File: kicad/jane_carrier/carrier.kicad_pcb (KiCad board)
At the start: 4 copper layers, 162.6 x 114.3 mm, 112 parts, among them CON1 EDSTL130_02, CON2 BNC_361V504EFT, CON3 BNC_361V504EFT, CON4 BNC_361V504EFT, CON5 BNC_361V504EFT, P1 61083-101400LF, P2 61083-101400LF, U1 STM6779LWB6F, U2 XCL214B333DR, U3 XCL214B333DR, U4 ADCMP552, U5 ADCMP552

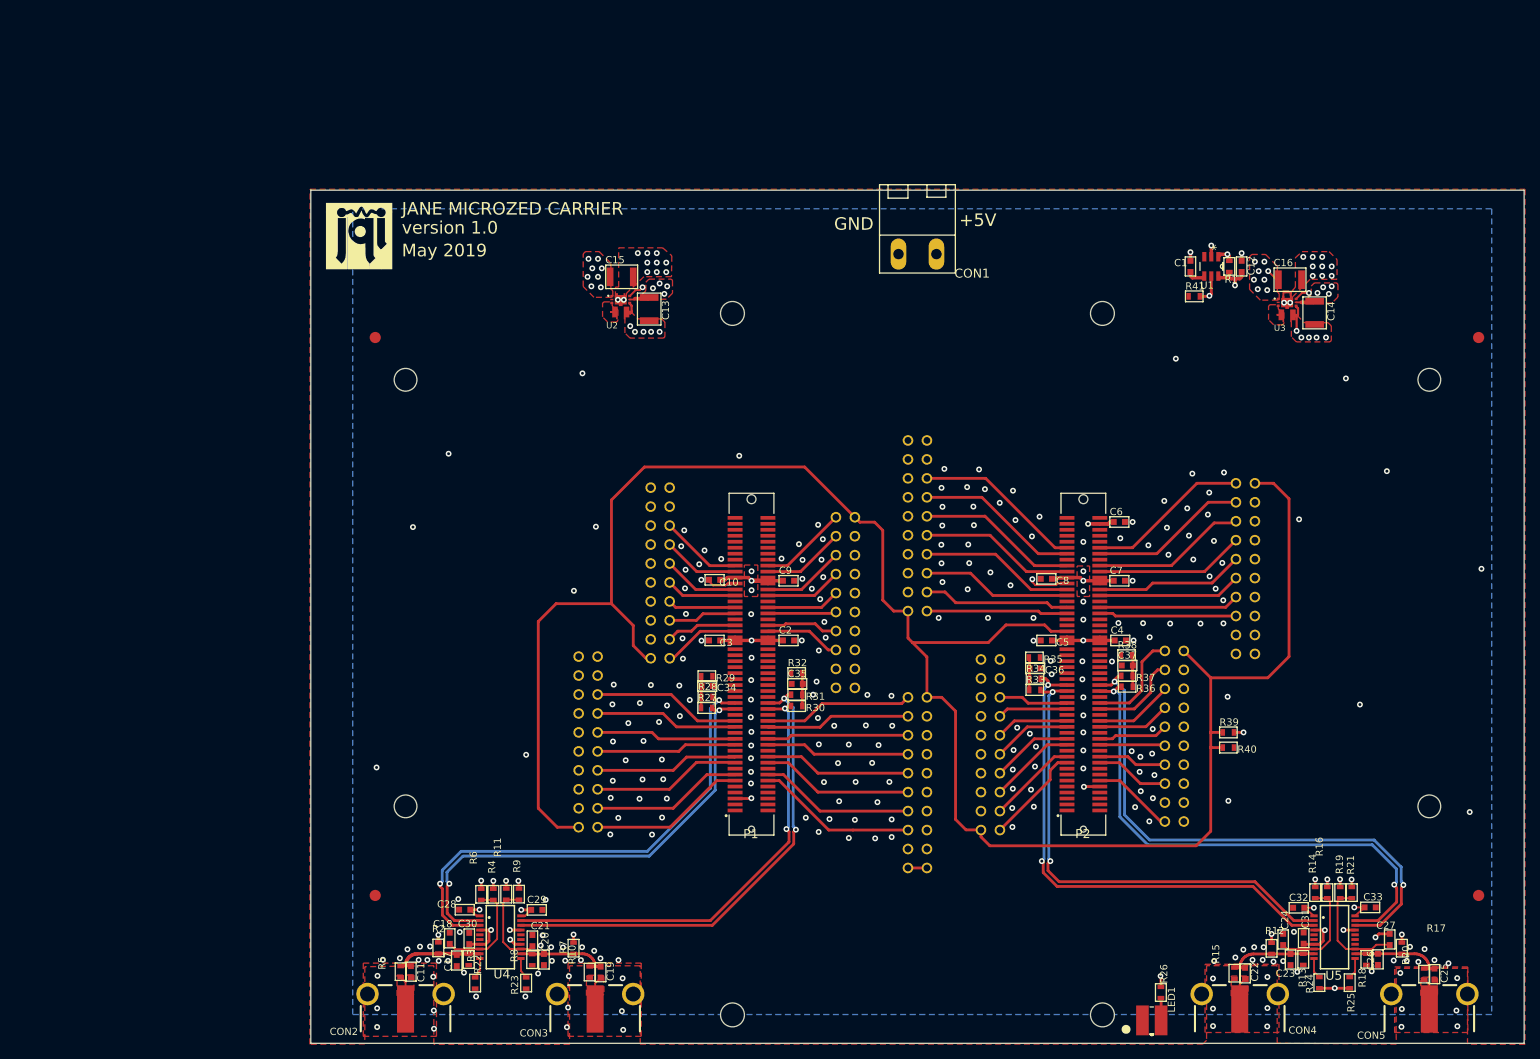
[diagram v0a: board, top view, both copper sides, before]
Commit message: Retouches to the silkscreen
Migrated to version 8 of Kicad.
gerber were generated and sent to fabrication.
Unfortunately the PCB file were overwritten before commiting, so the
current touches to the silkscreen are not isentical to the ones
submitted.
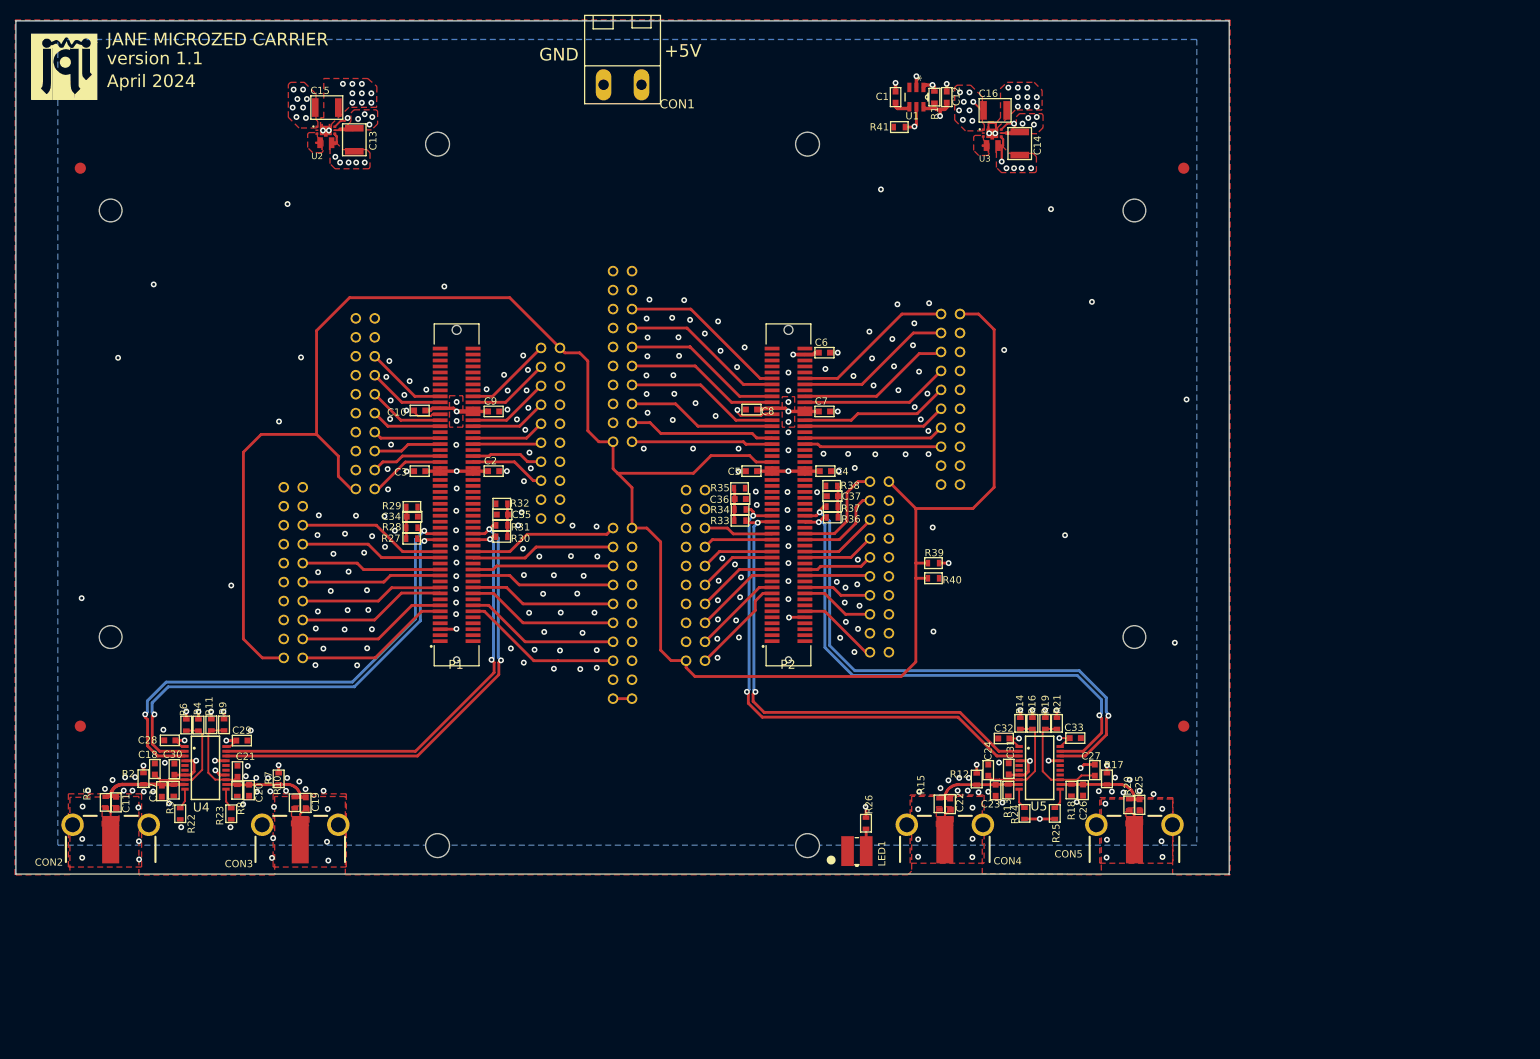
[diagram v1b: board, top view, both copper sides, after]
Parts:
- moved C1 45.6 mm to (145.6, 35.4)
- moved C12 45.6 mm to (152.4, 35.4)
- moved C13 45.6 mm to (73.1, 41.1)
- moved C31 45.6 mm to (160.7, 125.4)
- moved C32 45.6 mm to (160.1, 121.3)
- moved C37 45.6 mm to (137.1, 88.8)
- moved C4 45.6 mm to (136.2, 85.5)
- moved C6 45.6 mm to (136.0, 69.6)
- moved CON1 45.6 mm to (109.0, 33.7)
- moved FID4 45.6 mm to (184.2, 44.9)
- moved R17 45.6 mm to (173.9, 126.7)
- moved R33 45.6 mm to (124.7, 92.1)
- moved R38 45.6 mm to (137.0, 87.5)
- moved R39 45.6 mm to (150.6, 97.8)
- moved R40 45.6 mm to (150.6, 99.8)
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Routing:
- added copper zone on In1.Cu, net DGND
- added copper zone on In2.Cu, net DGND
- added copper zone on In2.Cu, net VCCIO_13_AND_35
- added copper zone on In2.Cu, net VCCIO_34
- removed copper zone on Route15, net DGND
- removed copper zone on Route2, net DGND
- removed copper zone on Route15, net VCCIO_13_AND_35
- removed copper zone on Route15, net VCCIO_34
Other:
- net class Default removed
- board text added: "April 2024"
- board text added: "version 1.1"
- board text removed: "May 2019"
- board text removed: "version 1.0"
